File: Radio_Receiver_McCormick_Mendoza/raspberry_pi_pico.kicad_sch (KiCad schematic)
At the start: 8 parts, among them J27 Conn_01x20_Socket, J28 Conn_01x01_Pin, J29 Conn_01x20_Socket, U4 Pico

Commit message: Updated footprints
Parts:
- J27: footprint Connector_PinSocket_2.54mm:PinSocket_1x20_P2.54mm_Vertical -> (none)
- J29: footprint Intro_to_CAD:PinSocket_1x20_P2.54mm_Vertical-pins21-40 -> (none)
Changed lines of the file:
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@@
+	)
+	(junction
+		(at 115.57 99.06)
+		(diameter 0)
+		(color 0 0 0 0)
+	)
+	(junction
+		(at 115.57 93.98)
+		(diameter 0)
+		(color 0 0 0 0)
+	)
+	(junction
+		(at 115.57 78.74)
+		(diameter 0)
+		(color 0 0 0 0)
+	)
+	(junction
+		(at 163.83 109.22)
+		(diameter 0)
+		(color 0 0 0 0)
+	)
+	(junction
+		(at 115.57 106.68)
+		(diameter 0)
+		(color 0 0 0 0)
+	)
+	(junction
+		(at 166.37 73.66)
+		(diameter 0)
+		(color 0 0 0 0)
+	)
+	(junction
+		(at 163.83 66.04)
+		(diameter 0)
+		(color 0 0 0 0)
+	)
+	(junction
+		(at 167.64 52.07)
+		(diameter 0)
+		(color 0 0 0 0)
+	)
+	(junction
+		(at 115.57 104.14)
+		(diameter 0)
+		(color 0 0 0 0)
+	)
+	(junction
+		(at 163.83 111.76)
+		(diameter 0)
+		(color 0 0 0 0)
+	)
+	(junction
+		(at 170.18 106.68)
+		(diameter 0)
+		(color 0 0 0 0)
+	)
+	(junction
+		(at 163.83 104.14)
+		(diameter 0)
+		(color 0 0 0 0)
+	)
+	(junction
+		(at 115.57 91.44)
+		(diameter 0)
+		(color 0 0 0 0)
+	)
+	(junction
+		(at 163.83 106.68)
+		(diameter 0)
+		(color 0 0 0 0)
+	)
+	(junction
+		(at 115.57 88.9)
+		(diameter 0)
+		(color 0 0 0 0)
+	)
+	(junction
+		(at 163.83 88.9)
+		(diameter 0)
+		(color 0 0 0 0)
+	)
+	(junction
+		(at 115.57 63.5)
+		(diameter 0)
+		(color 0 0 0 0)
+	)
+	(junction
+		(at 163.83 76.2)
+		(diameter 0)
+		(color 0 0 0 0)
+	)
+	(junction
+		(at 115.57 86.36)
+		(diameter 0)
+		(color 0 0 0 0)
+	)
+	(junction
+		(at 163.83 93.98)
+		(diameter 0)
+		(color 0 0 0 0)
+	)
+	(junction
+		(at 115.57 109.22)
+		(diameter 0)
+		(color 0 0 0 0)
+	)
+	(junction
+		(at 163.83 78.74)
+		(diameter 0)
+		(color 0 0 0 0)
+	)
+	(junction
+		(at 114.3 106.68)
+		(diameter 0)
+		(color 0 0 0 0)
+	)
+	(junction
+		(at 115.57 76.2)
+		(diameter 0)
+		(color 0 0 0 0)
 	)
 	(junction
@@
 	)
 	(junction
-		(at 115.57 99.06)
-		(diameter 0)
-		(color 0 0 0 0)
-	)
-	(junction
-		(at 163.83 109.22)
-		(diameter 0)
-		(color 0 0 0 0)
-	)
-	(junction
-		(at 166.37 73.66)
-		(diameter 0)
-		(color 0 0 0 0)
-	)
-	(junction
-		(at 115.57 91.44)
-		(diameter 0)
-		(color 0 0 0 0)
-	)
-	(junction
-		(at 163.83 66.04)
-		(diameter 0)
-		(color 0 0 0 0)
-	)
-	(junction
-		(at 167.64 52.07)
-		(diameter 0)
-		(color 0 0 0 0)
-	)
-	(junction
-		(at 163.83 111.76)
-		(diameter 0)
-		(color 0 0 0 0)
-	)
-	(junction
-		(at 170.18 106.68)
-		(diameter 0)
-		(color 0 0 0 0)
-	)
-	(junction
-		(at 163.83 104.14)
-		(diameter 0)
-		(color 0 0 0 0)
-	)
-	(junction
-		(at 163.83 106.68)
-		(diameter 0)
-		(color 0 0 0 0)
-	)
-	(junction
-		(at 115.57 63.5)
+		(at 115.57 71.12)
+		(diameter 0)
+		(color 0 0 0 0)
+	)
+	(junction
+		(at 186.69 58.42)
 		(diameter 0)
 		(color 0 0 0 0)
@@
 	)
 	(junction
-		(at 115.57 76.2)
-		(diameter 0)
-		(color 0 0 0 0)
-	)
-	(junction
-		(at 163.83 88.9)
+		(at 115.57 73.66)
+		(diameter 0)
+		(color 0 0 0 0)
+	)
+	(junction
+		(at 115.57 83.82)
+		(diameter 0)
+		(color 0 0 0 0)
+	)
+	(junction
+		(at 166.37 66.04)
+		(diameter 0)
+		(color 0 0 0 0)
+	)
+	(junction
+		(at 157.48 48.26)
+		(diameter 0)
+		(color 0 0 0 0)
+	)
+	(junction
+		(at 163.83 91.44)
+		(diameter 0)
+		(color 0 0 0 0)
+	)
+	(junction
+		(at 170.18 93.98)
+		(diameter 0)
+		(color 0 0 0 0)
+	)
+	(junction
+		(at 157.48 52.07)
+		(diameter 0)
+		(color 0 0 0 0)
+	)
+	(junction
+		(at 157.48 60.96)
+		(diameter 0)
+		(color 0 0 0 0)
+	)
+	(junction
+		(at 115.57 81.28)
+		(diameter 0)
+		(color 0 0 0 0)
+	)
+	(junction
+		(at 115.57 101.6)
+		(diameter 0)
+		(color 0 0 0 0)
+	)
+	(junction
+		(at 163.83 73.66)
+		(diameter 0)
+		(color 0 0 0 0)
+	)
+	(junction
+		(at 163.83 96.52)
+		(diameter 0)
+		(color 0 0 0 0)
+	)
+	(junction
+		(at 163.83 71.12)
+		(diameter 0)
+		(color 0 0 0 0)
+	)
+	(junction
+		(at 114.3 81.28)
+		(diameter 0)
+		(color 0 0 0 0)
+	)
+	(junction
+		(at 114.3 93.98)
+		(diameter 0)
+		(color 0 0 0 0)
+	)
+	(junction
+		(at 175.26 137.16)
+		(diameter 0)
+		(color 0 0 0 0)
+	)
+	(junction
+		(at 163.83 83.82)
+		(diameter 0)
+		(color 0 0 0 0)
+	)
+	(junction
+		(at 115.57 111.76)
+		(diameter 0)
+		(color 0 0 0 0)
+	)
+	(junction
+		(at 163.83 86.36)
 		(diameter 0)
 		(color 0 0 0 0)
@@
 	(junction
 		(at 115.57 66.04)
-		(diameter 0)
-		(color 0 0 0 0)
-	)
-	(junction
-		(at 163.83 76.2)
-		(diameter 0)
-		(color 0 0 0 0)
-	)
-	(junction
-		(at 115.57 88.9)
-		(diameter 0)
-		(color 0 0 0 0)
-	)
-	(junction
-		(at 115.57 93.98)
-		(diameter 0)
-		(color 0 0 0 0)
-	)
-	(junction
-		(at 163.83 93.98)
-		(diameter 0)
-		(color 0 0 0 0)
-	)
-	(junction
-		(at 163.83 78.74)
-		(diameter 0)
-		(color 0 0 0 0)
-	)
-	(junction
-		(at 114.3 106.68)
-		(diameter 0)
-		(color 0 0 0 0)
-	)
-	(junction
-		(at 115.57 71.12)
-		(diameter 0)
-		(color 0 0 0 0)
-	)
-	(junction
-		(at 115.57 111.76)
-		(diameter 0)
-		(color 0 0 0 0)
-	)
-	(junction
-		(at 186.69 58.42)
-		(diameter 0)
-		(color 0 0 0 0)
-	)
-	(junction
-		(at 115.57 78.74)
-		(diameter 0)
-		(color 0 0 0 0)
-	)
-	(junction
-		(at 166.37 66.04)
-		(diameter 0)
-		(color 0 0 0 0)
-	)
-	(junction
-		(at 115.57 83.82)
-		(diameter 0)
-		(color 0 0 0 0)
-	)
-	(junction
-		(at 157.48 48.26)
-		(diameter 0)
-		(color 0 0 0 0)
-	)
-	(junction
-		(at 163.83 91.44)
-		(diameter 0)
-		(color 0 0 0 0)
-	)
-	(junction
-		(at 170.18 93.98)
-		(diameter 0)
-		(color 0 0 0 0)
-	)
-	(junction
-		(at 157.48 52.07)
-		(diameter 0)
-		(color 0 0 0 0)
-	)
-	(junction
-		(at 115.57 109.22)
-		(diameter 0)
-		(color 0 0 0 0)
-	)
-	(junction
-		(at 157.48 60.96)
-		(diameter 0)
-		(color 0 0 0 0)
-	)
-	(junction
-		(at 115.57 101.6)
-		(diameter 0)
-		(color 0 0 0 0)
-	)
-	(junction
-		(at 115.57 73.66)
-		(diameter 0)
-		(color 0 0 0 0)
-	)
-	(junction
-		(at 163.83 73.66)
-		(diameter 0)
-		(color 0 0 0 0)
-	)
-	(junction
-		(at 163.83 96.52)
-		(diameter 0)
-		(color 0 0 0 0)
-	)
-	(junction
-		(at 163.83 71.12)
-		(diameter 0)
-		(color 0 0 0 0)
-	)
-	(junction
-		(at 114.3 81.28)
-		(diameter 0)
-		(color 0 0 0 0)
-	)
-	(junction
-		(at 115.57 86.36)
-		(diameter 0)
-		(color 0 0 0 0)
-	)
-	(junction
-		(at 115.57 106.68)
-		(diameter 0)
-		(color 0 0 0 0)
-	)
-	(junction
-		(at 114.3 93.98)
-		(diameter 0)
-		(color 0 0 0 0)
-	)
-	(junction
-		(at 175.26 137.16)
-		(diameter 0)
-		(color 0 0 0 0)
-	)
-	(junction
-		(at 115.57 104.14)
-		(diameter 0)
-		(color 0 0 0 0)
-	)
-	(junction
-		(at 163.83 83.82)
-		(diameter 0)
-		(color 0 0 0 0)
-	)
-	(junction
-		(at 115.57 81.28)
-		(diameter 0)
-		(color 0 0 0 0)
-	)
-	(junction
-		(at 163.83 86.36)
 		(diameter 0)
 		(color 0 0 0 0)
@@
 			)
 		)
-		(property "Footprint" "Intro_to_CAD:PinSocket_1x20_P2.54mm_Vertical-pins21-40"
+		(property "Footprint" ""
 			(at 158.75 86.36 0)
 			(hide yes)
@@
 			)
 		)
-		(property "Footprint" "Connector_PinSocket_2.54mm:PinSocket_1x20_P2.54mm_Vertical"
+		(property "Footprint" ""
 			(at 120.65 86.36 0)
 			(hide yes)

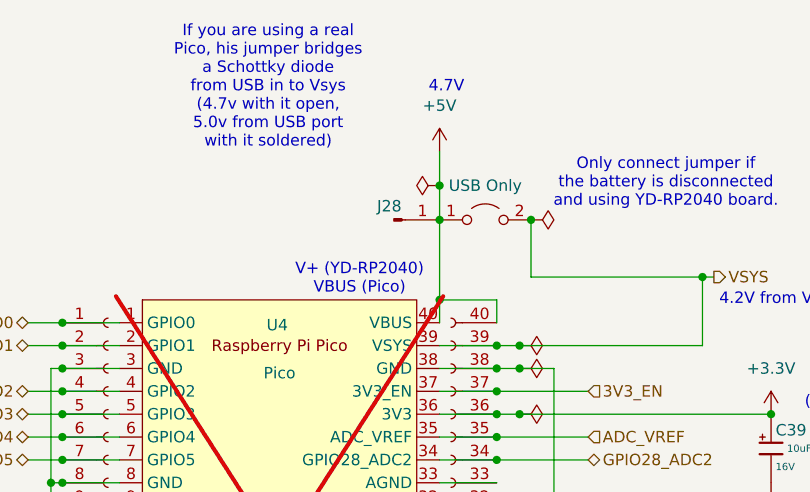
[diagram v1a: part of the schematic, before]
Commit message: Added pico and OLED arrangement to PCB
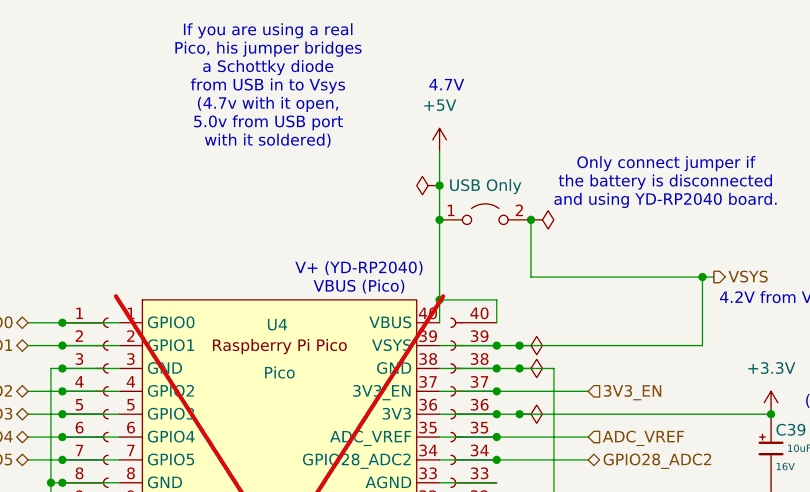
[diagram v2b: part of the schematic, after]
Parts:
- removed J28: Conn_01x01_Pin, Connector_PinHeader_2.54mm:PinHeader_1x01_P2.54mm_Vertical, symbol Connector:Conn_01x01_Pin
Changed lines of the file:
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@@
-	)
-	(symbol
-		(lib_id "Connector:Conn_01x01_Pin")
-		(at 152.4 52.07 0)
-		(unit 1)
-		(body_style 1)
-		(exclude_from_sim no)
-		(in_bom yes)
-		(on_board yes)
-		(in_pos_files yes)
-		(dnp no)
-		(property "Reference" "J28"
-			(at 151.892 50.546 0)
-			(show_name no)
-			(do_not_autoplace no)
-			(effects
-				(font
-					(size 1.27 1.27)
-				)
-			)
-		)
-		(property "Value" "Conn_01x01_Pin"
-			(at 153.035 49.53 0)
-			(hide yes)
-			(show_name no)
-			(do_not_autoplace no)
-			(effects
-				(font
-					(size 1.27 1.27)
-				)
-			)
-		)
-		(property "Footprint" "Connector_PinHeader_2.54mm:PinHeader_1x01_P2.54mm_Vertical"
-			(at 152.4 52.07 0)
-			(hide yes)
-			(show_name no)
-			(do_not_autoplace no)
-			(effects
-				(font
-					(size 1.27 1.27)
-				)
-			)
-		)
-		(property "Datasheet" ""
-			(at 152.4 52.07 0)
-			(hide yes)
-			(show_name no)
-			(do_not_autoplace no)
-			(effects
-				(font
-					(size 1.27 1.27)
-				)
-			)
-		)
-		(property "Description" "Generic connector, single row, 01x01, script generated"
-			(at 152.4 52.07 0)
-			(hide yes)
-			(show_name no)
-			(do_not_autoplace no)
-			(effects
-				(font
-					(size 1.27 1.27)
-				)
-			)
-		)
-		(pin "1"
-		)
-		(instances
-			(project "Radio_Receiver_McCormick_Mendoza"
-				(path "/f31d31ab-6846-4f3a-92b1-aa5a6a13373f/410b623f-becc-4f3c-a123-5075a8235689"
-					(reference "J28")
-					(unit 1)
-				)
-			)
-		)
 	)
 	(symbol
